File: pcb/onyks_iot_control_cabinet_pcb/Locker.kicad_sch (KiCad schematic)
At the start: 9 parts, among them J2 Screw_Terminal_01x02, J7 Conn_01x02_Socket, Q3 SQ4050EY-T1_GE3, Q4 SQ4050EY-T1_GE3, SW1 SW_Push

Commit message: New fixes of schematics
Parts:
- C3: value 0.1u -> 0.1u/50V; footprint Capacitor_SMD:C_0805_2012Metric -> Capacitor_SMD:C_0603_1608Metric
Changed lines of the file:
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@@
 			)
 		)
-		(property "Value" "0.1u"
+		(property "Value" "0.1u/50V"
 			(at 91.44 131.572 90)
 			(effects
@@
 			)
 		)
-		(property "Footprint" "Capacitor_SMD:C_0805_2012Metric"
+		(property "Footprint" "Capacitor_SMD:C_0603_1608Metric"
 			(at 96.2152 138.43 0)
 			(effects

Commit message: Quick Fixes
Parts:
- removed Q3, Q4: SQ4050EY-T1_GE3, ourFootprints:SOIC127P600X175-8N, symbol Simulation_SPICE:NMOS
- added D2, D3: S5J, Diode_SMD:D_SMC, symbol Diode:STTH212S
- added Q3, Q5: PMV100ENEAR, Package_TO_SOT_SMD:SOT-23, symbol Transistor_FET:2N7002
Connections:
- net +12V: now also D2.1 (K), D3.1 (K)
- net GND: now also Q3.2 (S), Q5.2 (S)
- net MCU_Buzzer_Switch: now also Q3.1 (G)
- net MCU_Locker_Switch: now also Q5.1 (G)
- net at J2.2 (Pin_2): now also D2.2 (A), Q5.3 (D)
- net at BZ1.A2 (-_2): now also D3.2 (A), Q3.3 (D)

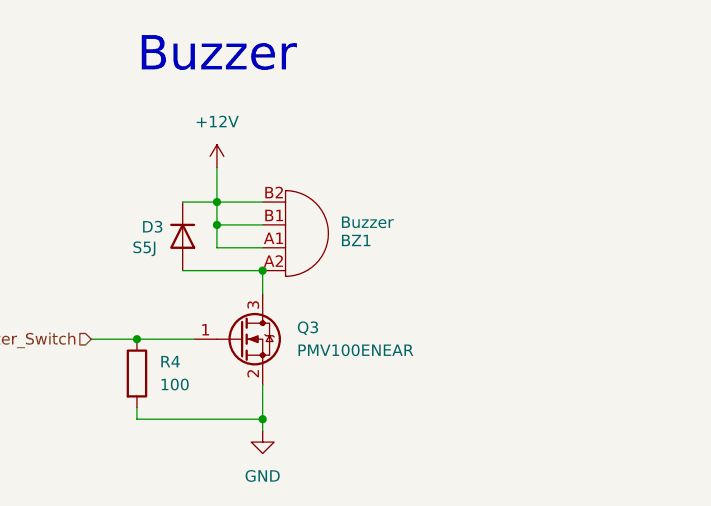
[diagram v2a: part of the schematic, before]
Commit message: Final fixes? - update the power supply
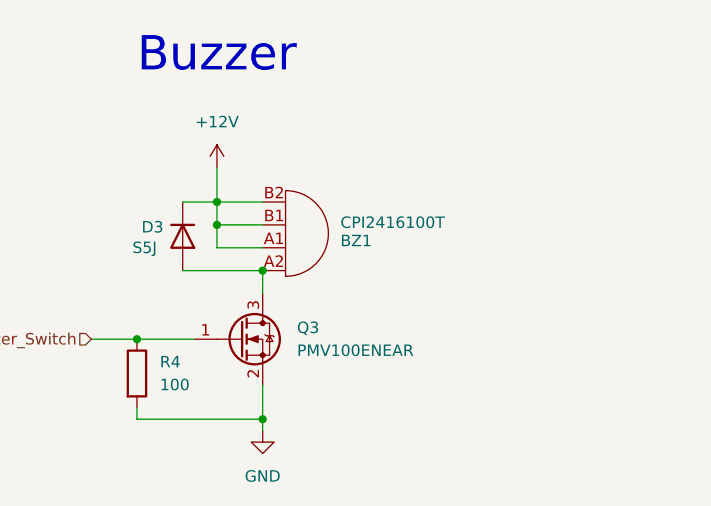
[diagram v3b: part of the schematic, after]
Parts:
- BZ1: value Buzzer -> CPI2416100T
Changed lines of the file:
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@@
 			)
 		)
-		(property "Value" "Buzzer"
+		(property "Value" "CPI2416100T"
 			(at 197.866 73.406 0)
 			(effects

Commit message: PCB Review 2.0 Update
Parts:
- removed D3: S5J, Diode_SMD:D_SMC, symbol Diode:STTH212S
- added R7: 100k, Resistor_SMD:R_0805_2012Metric_Pad1.20x1.40mm_HandSolder, symbol Device:R
- R3, R4: value 100 -> 100k
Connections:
- net +3.3V: no longer C3.1
- net GND: now also C3.2, R7.2
- net Locker_Manual_Switch: now also C3.1, R7.1; no longer C3.2
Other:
- moved on the sheet: C3, SW1

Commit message: Quick fixes
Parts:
- added R8: 240, Resistor_SMD:R_0805_2012Metric_Pad1.20x1.40mm_HandSolder, symbol Device:R
- R6: renamed from R7; value 100k -> 1k
- renumbered C3 to C10, J2 to J6, Q5 to Q3, Q3 to Q4, R3 to R5, R4 to R7, SW1 to SW3
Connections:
- net +12V: now also R8.1; no longer BZ1.A1 (-_1), BZ1.B1 (+_1), BZ1.B2 (+_2)
- new net: BZ1.A1 (-_1), BZ1.B1 (+_1), BZ1.B2 (+_2), R8.2
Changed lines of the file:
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@@
 	(text "Buzzer"
 		(exclude_from_sim no)
-		(at 184.15 54.864 0)
+		(at 184.15 53.34 0)
 		(effects
 			(font
@@
 	)
 	(junction
+		(at 184.15 71.12)
+		(diameter 0)
+		(color 0 0 0 0)
+	)
+	(junction
 		(at 110.49 91.44)
 		(diameter 0)
@@
 	)
 	(junction
-		(at 184.15 71.12)
-		(diameter 0)
-		(color 0 0 0 0)
-	)
-	(junction
 		(at 97.79 139.7)
 		(diameter 0)
@@
 	(wire
 		(pts
+			(xy 184.15 69.85) (xy 184.15 71.12)
+		)
+		(stroke
+			(width 0)
+			(type default)
+		)
+	)
+	(wire
+		(pts
 			(xy 110.49 73.66) (xy 110.49 77.47)
 		)
@@
 		(pts
 			(xy 97.79 139.7) (xy 97.79 142.24)
-		)
-		(stroke
-			(width 0)
-			(type default)
-		)
-	)
-	(wire
-		(pts
-			(xy 184.15 67.31) (xy 184.15 71.12)
 		)
 		(stroke
@@
 	)
 	(symbol
+		(lib_id "Device:R")
+		(at 184.15 66.04 0)
+		(unit 1)
+		(exclude_from_sim no)
+		(in_bom yes)
+		(on_board yes)
+		(dnp no)
+		(fields_autoplaced yes)
+		(property "Reference" "R8"
+			(at 186.69 64.7699 0)
+			(effects
+				(font
+					(size 1.27 1.27)
+				)
+				(justify left)
+			)
+		)
+		(property "Value" "240"
+			(at 186.69 67.3099 0)
+			(effects
+				(font
+					(size 1.27 1.27)
+				)
+				(justify left)
+			)
+		)
+		(property "Footprint" "Resistor_SMD:R_0805_2012Metric_Pad1.20x1.40mm_HandSolder"
+			(at 182.372 66.04 90)
+			(effects
+				(font
+					(size 1.27 1.27)
+				)
+				(hide yes)
+			)
+		)
+		(property "Datasheet" "~"
+			(at 184.15 66.04 0)
+			(effects
+				(font
+					(size 1.27 1.27)
+				)
+				(hide yes)
+			)
+		)
+		(property "Description" "Resistor"
+			(at 184.15 66.04 0)
+			(effects
+				(font
+					(size 1.27 1.27)
+				)
+				(hide yes)
+			)
+		)
+		(pin "2"
+		)
+		(pin "1"
+		)
+		(instances
+			(project "onyks_iot_control_cabinet_pcb"
+				(path "/789878cb-67d5-4bc7-a42d-b3bc72d661d0/48990703-11cc-42d8-8502-72244c0bfa20"
+					(reference "R8")
+					(unit 1)
+				)
+			)
+		)
+	)
+	(symbol
 		(lib_id "Connector:Screw_Terminal_01x02")
 		(at 115.57 71.12 0)
@@
 		(on_board yes)
 		(dnp no)
-		(property "Reference" "J2"
+		(property "Reference" "J6"
 			(at 118.11 71.1199 0)
 			(effects
@@
 			(project "onyks_iot_control_cabinet_pcb"
 				(path "/789878cb-67d5-4bc7-a42d-b3bc72d661d0/48990703-11cc-42d8-8502-72244c0bfa20"
-					(reference "J2")
+					(reference "J6")
 					(unit 1)
 				)
@@
 		(dnp no)
 		(fields_autoplaced yes)
-		(property "Reference" "#PWR010"
+		(property "Reference" "#PWR029"
 			(at 110.49 99.06 0)
 			(effects
@@
 			(project "onyks_iot_control_cabinet_pcb"
 				(path "/789878cb-67d5-4bc7-a42d-b3bc72d661d0/48990703-11cc-42d8-8502-72244c0bfa20"
-					(reference "#PWR010")
+					(reference "#PWR029")
 					(unit 1)
 				)
@@
 		(dnp no)
 		(fields_autoplaced yes)
-		(property "Reference" "#PWR09"
+		(property "Reference" "#PWR028"
 			(at 110.49 72.39 0)
 			(effects
@@
 			(project "onyks_iot_control_cabinet_pcb"
 				(path "/789878cb-67d5-4bc7-a42d-b3bc72d661d0/48990703-11cc-42d8-8502-72244c0bfa20"
-					(reference "#PWR09")
+					(reference "#PWR028")
 					(unit 1)
 				)
@@
 		(dnp no)
 		(fields_autoplaced yes)
-		(property "Reference" "#PWR030"
+		(property "Reference" "#PWR026"
 			(at 97.79 158.75 0)
 			(effects
@@
 			(project "onyks_iot_control_cabinet_pcb"
 				(path "/789878cb-67d5-4bc7-a42d-b3bc72d661d0/48990703-11cc-42d8-8502-72244c0bfa20"
-					(reference "#PWR030")
+					(reference "#PWR026")
 					(unit 1)
 				)
@@
 		(dnp no)
 		(fields_autoplaced yes)
-		(property "Reference" "Q5"
+		(property "Reference" "Q3"
 			(at 114.3 81.2799 0)
 			(effects
@@
 			(project ""
 				(path "/789878cb-67d5-4bc7-a42d-b3bc72d661d0/48990703-11cc-42d8-8502-72244c0bfa20"
-					(reference "Q5")
+					(reference "Q3")
 					(unit 1)
 				)
@@
 		(on_board yes)
 		(dnp no)
-		(property "Reference" "#PWR012"
+		(property "Reference" "#PWR030"
 			(at 113.03 128.27 0)
 			(effects
@@
 			(project "onyks_iot_control_cabinet_pcb"
 				(path "/789878cb-67d5-4bc7-a42d-b3bc72d661d0/48990703-11cc-42d8-8502-72244c0bfa20"
-					(reference "#PWR012")
+					(reference "#PWR030")
 					(unit 1)
 				)
@@
 		(dnp no)
 		(fields_autoplaced yes)
-		(property "Reference" "#PWR031"
+		(property "Reference" "#PWR027"
 			(at 109.22 158.75 0)
 			(effects
@@
 			(project "onyks_iot_control_cabinet_pcb"
 				(path "/789878cb-67d5-4bc7-a42d-b3bc72d661d0/48990703-11cc-42d8-8502-72244c0bfa20"
-					(reference "#PWR031")
+					(reference "#PWR027")
 					(unit 1)
 				)
@@
 		(dnp no)
 		(fields_autoplaced yes)
-		(property "Reference" "R3"
+		(property "Reference" "R5"
 			(at 99.06 85.0899 0)
 			(effects
@@
 			(project "onyks_iot_control_cabinet_pcb"
 				(path "/789878cb-67d5-4bc7-a42d-b3bc72d661d0/48990703-11cc-42d8-8502-72244c0bfa20"
-					(reference "R3")
+					(reference "R5")
 					(unit 1)
 				)
@@
 	(symbol
 		(lib_id "power:+12V")
-		(at 184.15 67.31 0)
+		(at 184.15 62.23 0)
 		(unit 1)
 		(exclude_from_sim no)
@@
 		(dnp no)
 		(fields_autoplaced yes)
-		(property "Reference" "#PWR013"
-			(at 184.15 71.12 0)
+		(property "Reference" "#PWR031"
+			(at 184.15 66.04 0)
 			(effects
 				(font
@@
 		)
 		(property "Value" "+12V"
+			(at 184.15 57.15 0)
+			(effects
+				(font
+					(size 1.27 1.27)
+				)
+			)
+		)
+		(property "Footprint" ""
 			(at 184.15 62.23 0)
 			(effects
@@
 					(size 1.27 1.27)
 				)
-			)
-		)
-		(property "Footprint" ""
-			(at 184.15 67.31 0)
-			(effects
-				(font
-					(size 1.27 1.27)
-				)
 				(hide yes)
 			)
 		)
 		(property "Datasheet" ""
-			(at 184.15 67.31 0)
+			(at 184.15 62.23 0)
 			(effects
 				(font
@@
 		)
 		(property "Description" "Power symbol creates a global label with name \"+12V\""
-			(at 184.15 67.31 0)
+			(at 184.15 62.23 0)
 			(effects
 				(font
@@
 			(project "onyks_iot_control_cabinet_pcb"
 				(path "/789878cb-67d5-4bc7-a42d-b3bc72d661d0/48990703-11cc-42d8-8502-72244c0bfa20"
-					(reference "#PWR013")
+					(reference "#PWR031")
 					(unit 1)
 				)
@@
 		(dnp no)
 		(fields_autoplaced yes)
-		(property "Reference" "R7"
+		(property "Reference" "R6"
 			(at 111.76 146.0499 0)
 			(effects
@@
 			)
 		)
-		(property "Value" "100k"
+		(property "Value" "1k"
 			(at 111.76 148.5899 0)
 			(effects
@@
 			(project "onyks_iot_control_cabinet_pcb"
 				(path "/789878cb-67d5-4bc7-a42d-b3bc72d661d0/48990703-11cc-42d8-8502-72244c0bfa20"
-					(reference "R7")
+					(reference "R6")
 					(unit 1)
 				)
@@
 		(dnp no)
 		(fields_autoplaced yes)
-		(property "Reference" "#PWR015"
+		(property "Reference" "#PWR032"
 			(at 189.23 102.87 0)
 			(effects
@@
 			(project "onyks_iot_control_cabinet_pcb"
 				(path "/789878cb-67d5-4bc7-a42d-b3bc72d661d0/48990703-11cc-42d8-8502-72244c0bfa20"
-					(reference "#PWR015")
+					(reference "#PWR032")
 					(unit 1)
 				)
@@
 		(on_board yes)
 		(dnp no)
-		(property "Reference" "#PWR011"
+		(property "Reference" "#PWR025"
 			(at 97.79 128.27 0)
 			(effects
@@
 			(project "onyks_iot_control_cabinet_pcb"
 				(path "/789878cb-67d5-4bc7-a42d-b3bc72d661d0/48990703-11cc-42d8-8502-72244c0bfa20"
-					(reference "#PWR011")
+					(reference "#PWR025")
 					(unit 1)
 				)
@@
 		(dnp no)
 		(fields_autoplaced yes)
-		(property "Reference" "R4"
+		(property "Reference" "R7"
 			(at 177.8 88.8999 0)
 			(effects
@@
 			(project "onyks_iot_control_cabinet_pcb"
 				(path "/789878cb-67d5-4bc7-a42d-b3bc72d661d0/48990703-11cc-42d8-8502-72244c0bfa20"
-					(reference "R4")
+					(reference "R7")
 					(unit 1)
 				)
@@
 		(dnp no)
 		(fields_autoplaced yes)
-		(property "Reference" "SW1"
+		(property "Reference" "SW3"
 			(at 105.41 134.62 0)
 			(effects
@@
 			(project "onyks_iot_control_cabinet_pcb"
 				(path "/789878cb-67d5-4bc7-a42d-b3bc72d661d0/48990703-11cc-42d8-8502-72244c0bfa20"
-					(reference "SW1")
+					(reference "SW3")
 					(unit 1)
 				)
@@
 		(on_board yes)
 		(dnp no)
-		(property "Reference" "C3"
+		(property "Reference" "C10"
 			(at 101.6 146.05 90)
 			(effects
@@
 			(project "onyks_iot_control_cabinet_pcb"
 				(path "/789878cb-67d5-4bc7-a42d-b3bc72d661d0/48990703-11cc-42d8-8502-72244c0bfa20"
-					(reference "C3")
+					(reference "C10")
 					(unit 1)
 				)
@@
 		(dnp no)
 		(fields_autoplaced yes)
-		(property "Reference" "Q3"
+		(property "Reference" "Q4"
 			(at 193.04 85.0899 0)
 			(effects
@@
 			(project "onyks_iot_control_cabinet_pcb"
 				(path "/789878cb-67d5-4bc7-a42d-b3bc72d661d0/48990703-11cc-42d8-8502-72244c0bfa20"
-					(reference "Q3")
-					(unit 1)
-				)
+					(reference "Q4")
+					(unit 1)
+				)

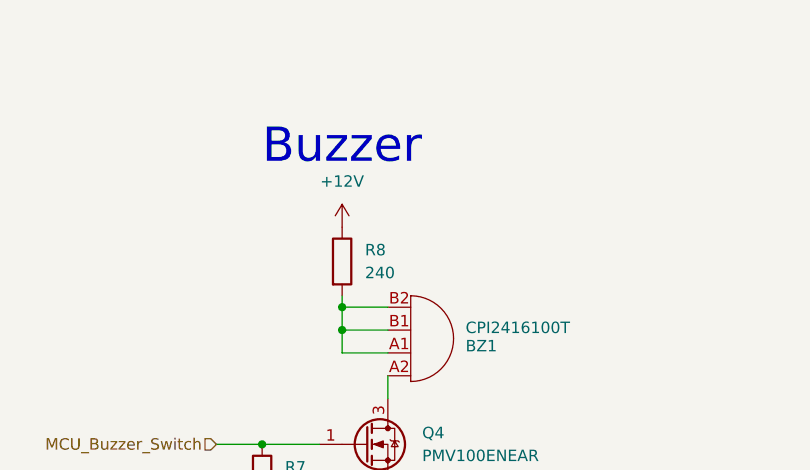
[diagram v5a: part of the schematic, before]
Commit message: Update the PCB and schematics; add the potentiometer
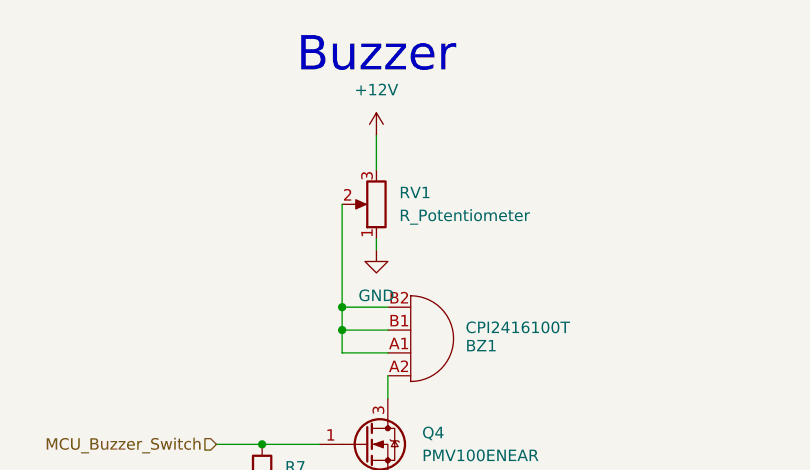
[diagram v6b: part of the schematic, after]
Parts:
- removed R8: 240, Resistor_SMD:R_0805_2012Metric_Pad1.20x1.40mm_HandSolder, symbol Device:R
- added RV1: R_Potentiometer, Potentiometer_THT:Potentiometer_Vishay_T73YP_Vertical, symbol Device:R_Potentiometer
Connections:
- net +12V: now also RV1.3
- net GND: now also RV1.1
- net at BZ1.A1 (-_1), BZ1.B1 (+_1), BZ1.B2 (+_2): now also RV1.2
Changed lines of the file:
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@@
 	(text "Buzzer"
 		(exclude_from_sim no)
-		(at 184.15 53.34 0)
+		(at 187.96 43.18 0)
 		(effects
 			(font
@@
 	(wire
 		(pts
+			(xy 187.96 63.5) (xy 187.96 64.77)
+		)
+		(stroke
+			(width 0)
+			(type default)
+		)
+	)
+	(wire
+		(pts
 			(xy 175.26 86.36) (xy 181.61 86.36)
 		)
@@
 	(wire
 		(pts
-			(xy 184.15 69.85) (xy 184.15 71.12)
+			(xy 184.15 59.69) (xy 184.15 71.12)
 		)
 		(stroke
@@
 		(pts
 			(xy 110.49 73.66) (xy 110.49 77.47)
+		)
+		(stroke
+			(width 0)
+			(type default)
+		)
+	)
+	(wire
+		(pts
+			(xy 187.96 52.07) (xy 187.96 55.88)
 		)
 		(stroke
@@
 	)
 	(symbol
-		(lib_id "Device:R")
-		(at 184.15 66.04 0)
-		(unit 1)
-		(exclude_from_sim no)
-		(in_bom yes)
-		(on_board yes)
-		(dnp no)
-		(fields_autoplaced yes)
-		(property "Reference" "R8"
-			(at 186.69 64.7699 0)
-			(effects
-				(font
-					(size 1.27 1.27)
-				)
-				(justify left)
-			)
-		)
-		(property "Value" "240"
-			(at 186.69 67.3099 0)
-			(effects
-				(font
-					(size 1.27 1.27)
-				)
-				(justify left)
-			)
-		)
-		(property "Footprint" "Resistor_SMD:R_0805_2012Metric_Pad1.20x1.40mm_HandSolder"
-			(at 182.372 66.04 90)
-			(effects
-				(font
-					(size 1.27 1.27)
-				)
-				(hide yes)
-			)
-		)
-		(property "Datasheet" "~"
-			(at 184.15 66.04 0)
-			(effects
-				(font
-					(size 1.27 1.27)
-				)
-				(hide yes)
-			)
-		)
-		(property "Description" "Resistor"
-			(at 184.15 66.04 0)
-			(effects
-				(font
-					(size 1.27 1.27)
-				)
-				(hide yes)
-			)
-		)
-		(pin "2"
-		)
-		(pin "1"
-		)
-		(instances
-			(project "onyks_iot_control_cabinet_pcb"
-				(path "/789878cb-67d5-4bc7-a42d-b3bc72d661d0/48990703-11cc-42d8-8502-72244c0bfa20"
-					(reference "R8")
-					(unit 1)
-				)
-			)
-		)
-	)
-	(symbol
 		(lib_id "Connector:Screw_Terminal_01x02")
 		(at 115.57 71.12 0)
@@
 		(lib_name "GND_1")
 		(lib_id "power:GND")
+		(at 187.96 64.77 0)
+		(unit 1)
+		(exclude_from_sim no)
+		(in_bom yes)
+		(on_board yes)
+		(dnp no)
+		(fields_autoplaced yes)
+		(property "Reference" "#PWR036"
+			(at 187.96 71.12 0)
+			(effects
+				(font
+					(size 1.27 1.27)
+				)
+				(hide yes)
+			)
+		)
+		(property "Value" "GND"
+			(at 187.96 69.85 0)
+			(effects
+				(font
+					(size 1.27 1.27)
+				)
+			)
+		)
+		(property "Footprint" ""
+			(at 187.96 64.77 0)
+			(effects
+				(font
+					(size 1.27 1.27)
+				)
+				(hide yes)
+			)
+		)
+		(property "Datasheet" ""
+			(at 187.96 64.77 0)
+			(effects
+				(font
+					(size 1.27 1.27)
+				)
+				(hide yes)
+			)
+		)
+		(property "Description" "Power symbol creates a global label with name \"GND\" , ground"
+			(at 187.96 64.77 0)
+			(effects
+				(font
+					(size 1.27 1.27)
+				)
+				(hide yes)
+			)
+		)
+		(pin "1"
+		)
+		(instances
+			(project "onyks_iot_control_cabinet_pcb"
+				(path "/789878cb-67d5-4bc7-a42d-b3bc72d661d0/48990703-11cc-42d8-8502-72244c0bfa20"
+					(reference "#PWR036")
+					(unit 1)
+				)
+			)
+		)
+	)
+	(symbol
+		(lib_name "GND_1")
+		(lib_id "power:GND")
 		(at 97.79 152.4 0)
 		(unit 1)
@@
 	(symbol
 		(lib_id "power:+12V")
-		(at 184.15 62.23 0)
+		(at 187.96 52.07 0)
 		(unit 1)
 		(exclude_from_sim no)
@@
 		(fields_autoplaced yes)
 		(property "Reference" "#PWR031"
-			(at 184.15 66.04 0)
+			(at 187.96 55.88 0)
 			(effects
 				(font
@@
 		)
 		(property "Value" "+12V"
-			(at 184.15 57.15 0)
+			(at 187.96 46.99 0)
 			(effects
 				(font
@@
 		)
 		(property "Footprint" ""
-			(at 184.15 62.23 0)
+			(at 187.96 52.07 0)
 			(effects
 				(font
@@
 		)
 		(property "Datasheet" ""
-			(at 184.15 62.23 0)
+			(at 187.96 52.07 0)
 			(effects
 				(font
@@
 		)
 		(property "Description" "Power symbol creates a global label with name \"+12V\""
-			(at 184.15 62.23 0)
+			(at 187.96 52.07 0)
 			(effects
 				(font
@@
 					(unit 1)
 				)
+			)
+		)
+	)
+	(symbol
+		(lib_id "Device:R_Potentiometer")
+		(at 187.96 59.69 180)
+		(unit 1)
+		(exclude_from_sim no)
+		(in_bom yes)
+		(on_board yes)
+		(dnp no)
+		(fields_autoplaced yes)
+		(property "Reference" "RV1"
+			(at 190.5 58.4199 0)
+			(effects
+				(font
+					(size 1.27 1.27)
+				)
+				(justify right)
+			)
+		)
+		(property "Value" "R_Potentiometer"
+			(at 190.5 60.9599 0)
+			(effects
+				(font
+					(size 1.27 1.27)
+				)
+				(justify right)
+			)
+		)
+		(property "Footprint" "Potentiometer_THT:Potentiometer_Vishay_T73YP_Vertical"
+			(at 187.96 59.69 0)
+			(effects
+				(font
+					(size 1.27 1.27)
+				)
+				(hide yes)
+			)
+		)
+		(property "Datasheet" "~"
+			(at 187.96 59.69 0)
+			(effects
+				(font
+					(size 1.27 1.27)
+				)
+				(hide yes)
+			)
+		)
+		(property "Description" "Potentiometer"
+			(at 187.96 59.69 0)
+			(effects
+				(font
+					(size 1.27 1.27)
+				)
+				(hide yes)
+			)
+		)
+		(pin "2"
+		)
+		(pin "3"
+		)
+		(pin "1"
+		)
+		(instances
+			(project "onyks_iot_control_cabinet_pcb"
+				(path "/789878cb-67d5-4bc7-a42d-b3bc72d661d0/48990703-11cc-42d8-8502-72244c0bfa20"
+					(reference "RV1")
+					(unit 1)
+				)
